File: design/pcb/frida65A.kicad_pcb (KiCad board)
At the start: 4 copper layers, 100 x 100 mm, 105 parts, among them J1 DisplayPort Molex 472720024, J10 VIN CFG, J11 TP AMP, J12 MiniFitJr Molex 469990014, J13 POWER, J14 RJ45 Molex 446200002, J15 SPI TP, J2 TP CLOCKS, J3 SMA Molex 733910070, J4 SMA Molex 733910070, J5 DIFF/SE CFG, J6 TERM CFG, J7 ATTEN CFG, J8 SMA Molex 733910070, J9 TERM CFG, Q1 Q_PMOS_DGS, U1 DiffAmp TI THS4541, U2 TI LevelShifter SN74AXC8T245R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, U3 ASIC FRIDA 65A

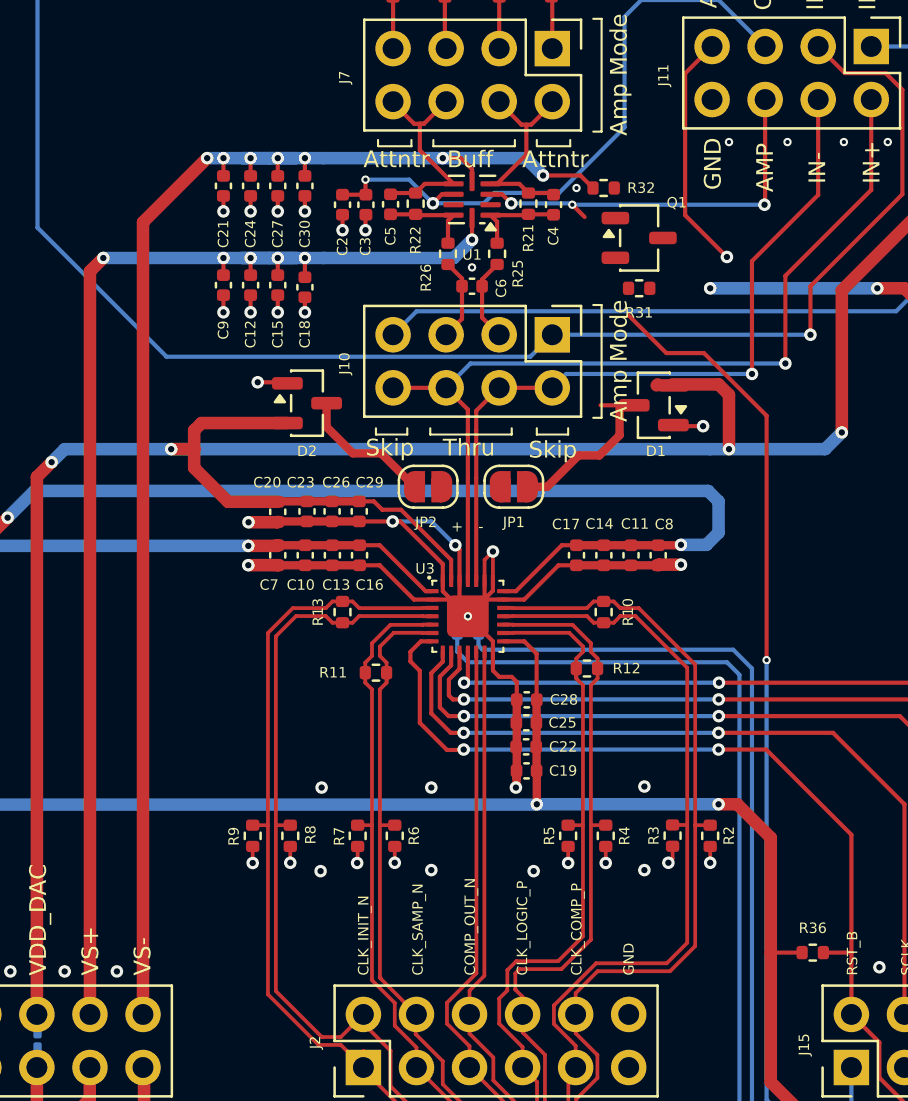
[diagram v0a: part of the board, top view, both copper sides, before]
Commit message: docs: add ADC measurement slide deck
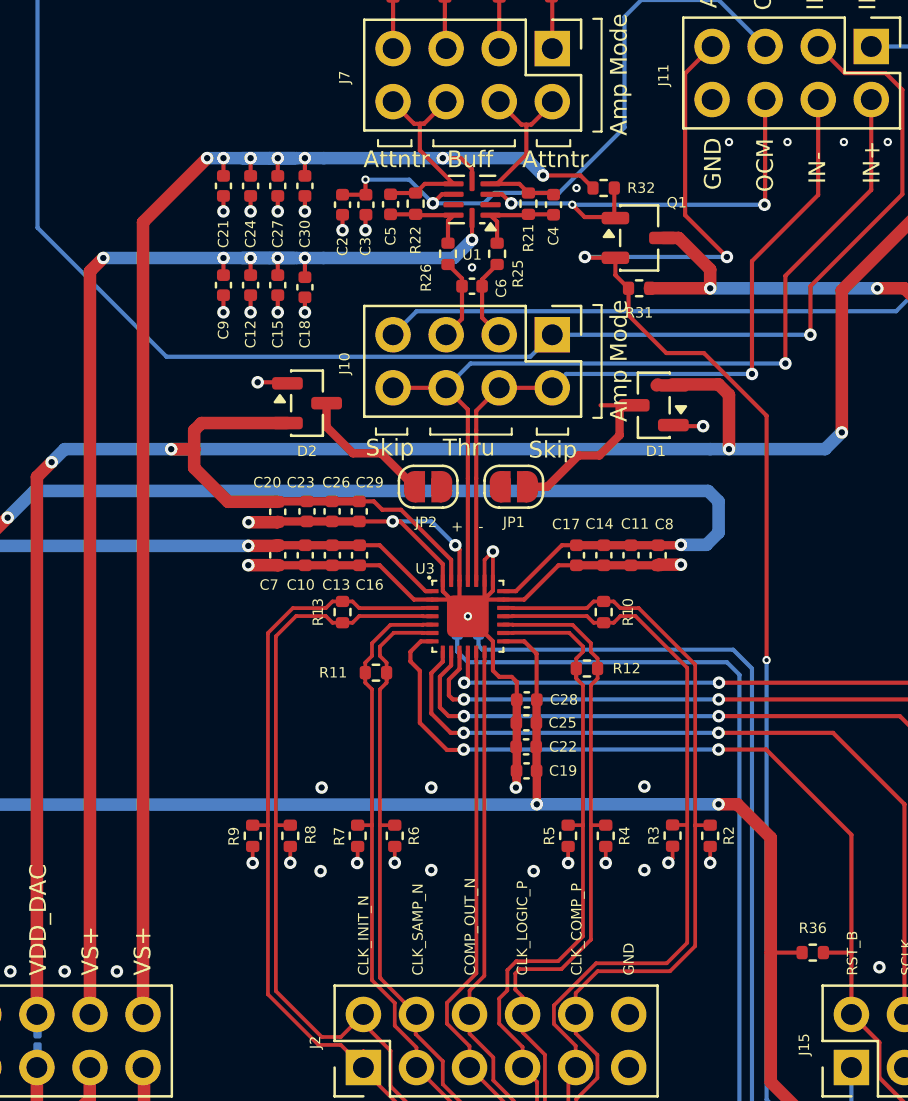
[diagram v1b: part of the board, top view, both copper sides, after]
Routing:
- net /AMP_PD_EXT: track 73.4 -> 84.7 mm, vias 3 -> 4
- net /VDD_BDAQ: track 105.5 -> 112.2 mm
- net /AMP_PD_N: track 19.3 -> 22.2 mm
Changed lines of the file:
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@@
 		)
 	)
-	(gr_text "AMP"
+	(gr_text "OCM"
 		(at 164.7 79.6 90)
 		(layer "F.SilkS")
@@
 		)
 	)
-	(gr_text "VS-"
+	(gr_text "VS+"
 		(at 134.9 117.1 90)
 		(layer "F.SilkS")
@@
 	)
 	(segment
+		(start 161.6 84.2)
+		(end 158.71 84.2)
+		(width 0.6)
+		(layer "F.Cu")
+		(net 58)
+	)
+	(segment
+		(start 160.09 81.79)
+		(end 159.3375 81.79)
+		(width 0.6)
+		(layer "F.Cu")
+		(net 58)
+	)
+	(segment
 		(start 172.11 128.29)
 		(end 173 128.29)
@@
 	)
 	(segment
+		(start 161.6 84.2)
+		(end 161.6 83.3)
+		(width 0.6)
+		(layer "F.Cu")
+		(net 58)
+	)
+	(segment
+		(start 161.6 83.3)
+		(end 160.09 81.79)
+		(width 0.6)
+		(layer "F.Cu")
+		(net 58)
+	)
+	(segment
 		(start 170.38 130.4)
 		(end 171.388 130.4)
@@
 	)
 	(segment
+		(start 155.64 82.74)
+		(end 155.6 82.7)
+		(width 0.2)
+		(layer "F.Cu")
+		(net 59)
+	)
+	(segment
 		(start 160.4 73.915)
 		(end 161.69 72.625)
@@
 	)
 	(segment
+		(start 157.69 85.49)
+		(end 157.69 84.2)
+		(width 0.2)
+		(layer "F.Cu")
+		(net 59)
+	)
+	(segment
 		(start 161.3 87.3)
 		(end 159.5 87.3)
@@
 	)
 	(segment
+		(start 157.0625 82.74)
+		(end 155.64 82.74)
+		(width 0.2)
+		(layer "F.Cu")
+		(net 59)
+	)
+	(segment
 		(start 159.5 87.3)
 		(end 157.69 85.49)
@@
 	)
 	(segment
+		(start 157.0625 83.5725)
+		(end 157.69 84.2)
+		(width 0.2)
+		(layer "F.Cu")
+		(net 59)
+	)
+	(segment
 		(start 173.42 139.8585)
 		(end 173.42 132.42)
@@
 		(net 59)
 	)
+	(segment
+		(start 157.0625 82.74)
+		(end 157.0625 83.5725)
+		(width 0.2)
+		(layer "F.Cu")
+		(net 59)
+	)
+	(via
+		(at 155.6 82.7)
+		(size 0.6)
+		(drill 0.3)
+		(layers "F.Cu" "B.Cu")
+		(net 59)
+	)
 	(via
 		(at 162.4 82.7)
@@
 	)
 	(segment
+		(start 155.6 82.7)
+		(end 162.4 82.7)
+		(width 0.2)
+		(layer "B.Cu")
+		(net 59)
+	)
+	(segment
 		(start 164.3 123.041479)
 		(end 164.3 102)
@@
 		(width 0.2)
 		(layer "F.Cu")
+		(net 60)
+	)
+	(segment
+		(start 157.0125 80.79)
+		(end 155.59 80.79)
+		(width 0.2)
+		(layer "F.Cu")
+		(net 60)
+	)
+	(segment
+		(start 157.01 79.4)
+		(end 157.01 80.7875)
+		(width 0.2)
+		(layer "F.Cu")

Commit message: chore(pcb): update schematic and layout
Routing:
- net /AMP_PD_EXT: track 84.7 -> 73.4 mm, vias 4 -> 3
- net /VDD_BDAQ: track 112.2 -> 105.5 mm
- net /AMP_PD_N: track 22.2 -> 19.3 mm
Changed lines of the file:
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@@
 		)
 	)
-	(gr_text "OCM"
+	(gr_text "AMP"
 		(at 164.7 79.6 90)
 		(layer "F.SilkS")
@@
 		)
 	)
-	(gr_text "VS+"
+	(gr_text "VS-"
 		(at 134.9 117.1 90)
 		(layer "F.SilkS")
@@
 	)
 	(segment
-		(start 161.6 84.2)
-		(end 158.71 84.2)
-		(width 0.6)
-		(layer "F.Cu")
-		(net 58)
-	)
-	(segment
-		(start 160.09 81.79)
-		(end 159.3375 81.79)
-		(width 0.6)
-		(layer "F.Cu")
-		(net 58)
-	)
-	(segment
 		(start 172.11 128.29)
 		(end 173 128.29)
@@
 	)
 	(segment
-		(start 161.6 84.2)
-		(end 161.6 83.3)
-		(width 0.6)
-		(layer "F.Cu")
-		(net 58)
-	)
-	(segment
-		(start 161.6 83.3)
-		(end 160.09 81.79)
-		(width 0.6)
-		(layer "F.Cu")
-		(net 58)
-	)
-	(segment
 		(start 170.38 130.4)
 		(end 171.388 130.4)
@@
 	)
 	(segment
-		(start 155.64 82.74)
-		(end 155.6 82.7)
-		(width 0.2)
-		(layer "F.Cu")
-		(net 59)
-	)
-	(segment
 		(start 160.4 73.915)
 		(end 161.69 72.625)
@@
 	)
 	(segment
-		(start 157.69 85.49)
-		(end 157.69 84.2)
-		(width 0.2)
-		(layer "F.Cu")
-		(net 59)
-	)
-	(segment
 		(start 161.3 87.3)
 		(end 159.5 87.3)
@@
 	)
 	(segment
-		(start 157.0625 82.74)
-		(end 155.64 82.74)
-		(width 0.2)
-		(layer "F.Cu")
-		(net 59)
-	)
-	(segment
 		(start 159.5 87.3)
 		(end 157.69 85.49)
@@
 	)
 	(segment
-		(start 157.0625 83.5725)
-		(end 157.69 84.2)
-		(width 0.2)
-		(layer "F.Cu")
-		(net 59)
-	)
-	(segment
 		(start 173.42 139.8585)
 		(end 173.42 132.42)
@@
 		(net 59)
 	)
-	(segment
-		(start 157.0625 82.74)
-		(end 157.0625 83.5725)
-		(width 0.2)
-		(layer "F.Cu")
-		(net 59)
-	)
-	(via
-		(at 155.6 82.7)
-		(size 0.6)
-		(drill 0.3)
-		(layers "F.Cu" "B.Cu")
-		(net 59)
-	)
 	(via
 		(at 162.4 82.7)
@@
 	)
 	(segment
-		(start 155.6 82.7)
-		(end 162.4 82.7)
-		(width 0.2)
-		(layer "B.Cu")
-		(net 59)
-	)
-	(segment
 		(start 164.3 123.041479)
 		(end 164.3 102)
@@
 		(width 0.2)
 		(layer "F.Cu")
-		(net 60)
-	)
-	(segment
-		(start 157.0125 80.79)
-		(end 155.59 80.79)
-		(width 0.2)
-		(layer "F.Cu")
-		(net 60)
-	)
-	(segment
-		(start 157.01 79.4)
-		(end 157.01 80.7875)
-		(width 0.2)
-		(layer "F.Cu")
